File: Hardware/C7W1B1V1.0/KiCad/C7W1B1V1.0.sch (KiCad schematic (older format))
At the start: 2 parts

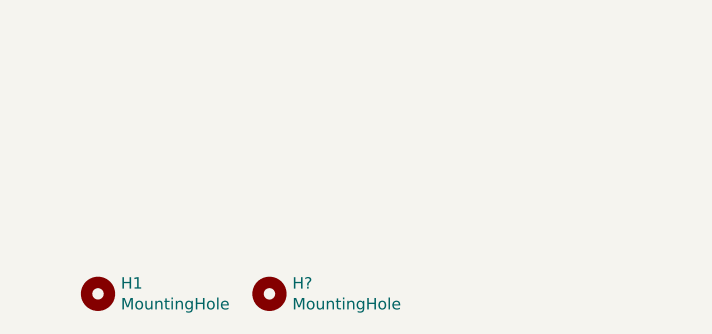
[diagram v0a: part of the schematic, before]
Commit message: Zmieniono procesor na wersję LQFP-64
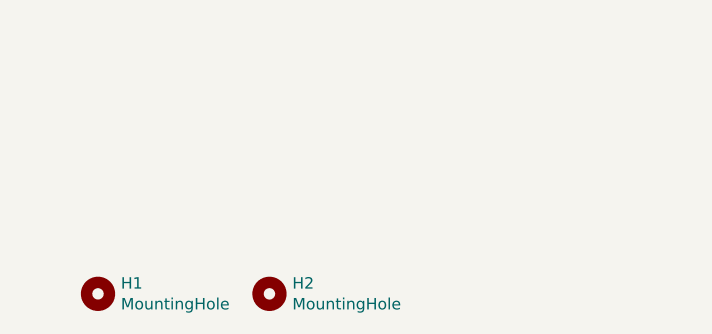
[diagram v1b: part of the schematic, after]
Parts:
- gave numbers to parts that had none: 1
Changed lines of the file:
@@
 $EndComp
 $Comp
-L Mechanical:MountingHole H?
+L Mechanical:MountingHole H2
 U 1 1 675AA29B
 P 2100 6900
-F 0 "H?" H 2200 6946 50  0000 L CNN
+F 0 "H2" H 2200 6946 50  0000 L CNN
 F 1 "MountingHole" H 2200 6855 50  0000 L CNN
 F 2 "MountingHole:MountingHole_2.7mm_M2.5" H 2100 6900 50  0001 C CNN
